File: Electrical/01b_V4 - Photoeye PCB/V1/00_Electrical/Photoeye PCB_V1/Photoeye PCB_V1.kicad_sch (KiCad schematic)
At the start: 13 parts, among them J1 B3B-PH-SM4-TB(LF)(SN), J2 B3B-PH-SM4-TB(LF)(SN), U1 LM293ST, U2 RPR-220

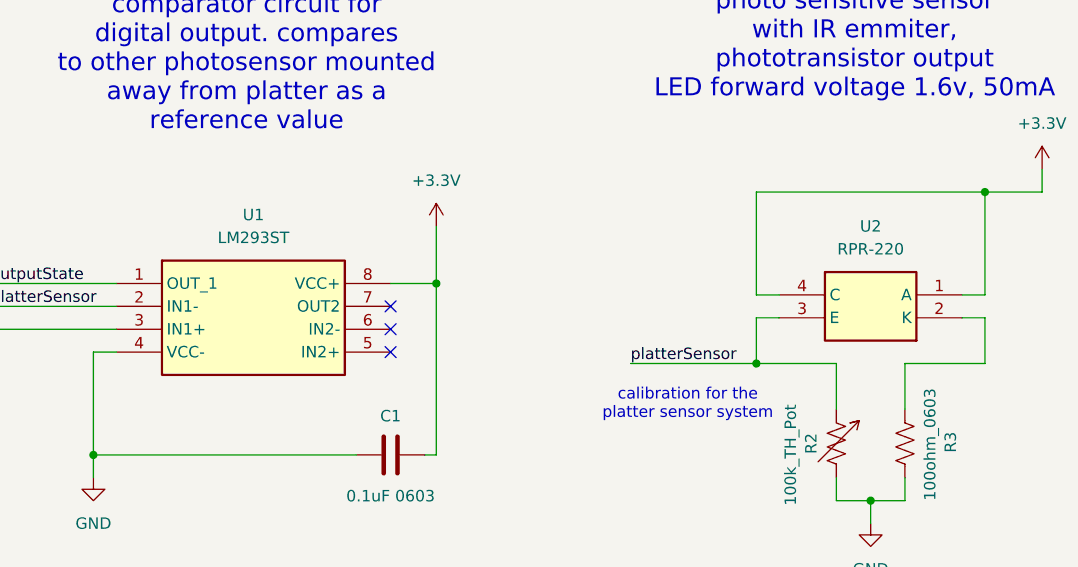
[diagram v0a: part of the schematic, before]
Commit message: fixing the crossed wire for the photo sensor. deleting the old CNC jobs. Re-exporting gerbers and schematics. Re-mill with new files
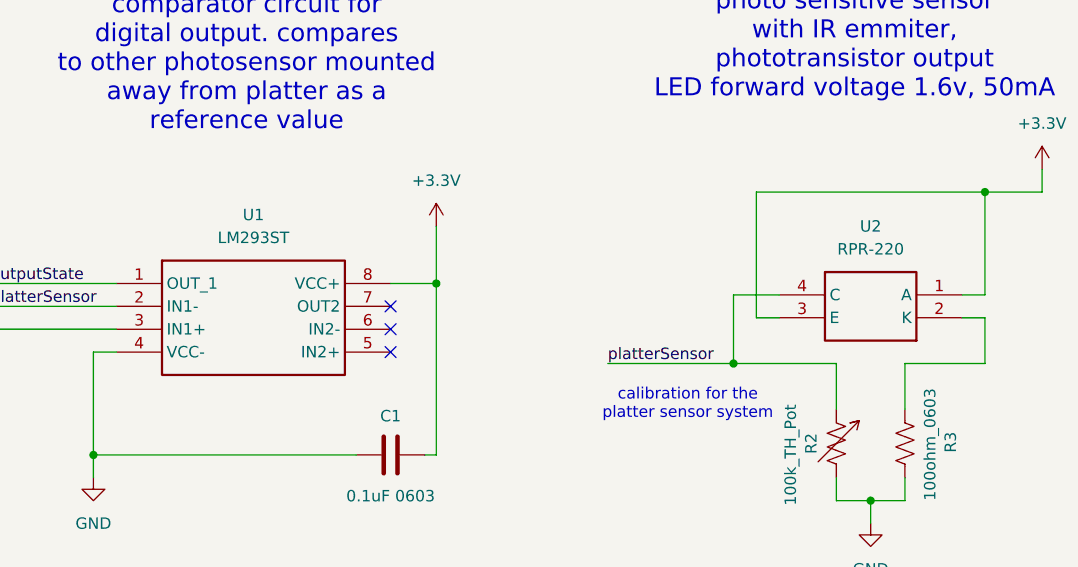
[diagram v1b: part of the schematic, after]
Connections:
- net +3.3V: now also U2.3 (E); no longer U2.4 (C)
- net platterSensor: now also U2.4 (C); no longer U2.3 (E)
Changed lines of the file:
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@@
 	)
 	(junction
-		(at 198.12 68.58)
+		(at 170.18 87.63)
 		(diameter 0)
 		(color 0 0 0 0)
 	)
 	(junction
-		(at 172.72 87.63)
+		(at 198.12 68.58)
 		(diameter 0)
 		(color 0 0 0 0)
@@
 	(wire
 		(pts
+			(xy 172.72 82.55) (xy 175.26 82.55)
+		)
+		(stroke
+			(width 0)
+			(type default)
+		)
+	)
+	(wire
+		(pts
 			(xy 227.33 81.28) (xy 227.33 86.36)
 		)
@@
 	(wire
 		(pts
-			(xy 101.6 86.36) (xy 99.06 86.36)
+			(xy 172.72 68.58) (xy 172.72 82.55)
 		)
 		(stroke
@@
 	(wire
 		(pts
-			(xy 238.76 60.96) (xy 238.76 73.66)
+			(xy 101.6 86.36) (xy 99.06 86.36)
 		)
 		(stroke
@@
 	(wire
 		(pts
-			(xy 49.53 76.2) (xy 49.53 71.12)
+			(xy 238.76 60.96) (xy 238.76 73.66)
 		)
 		(stroke
@@
 	(wire
 		(pts
-			(xy 172.72 87.63) (xy 181.61 87.63)
+			(xy 49.53 76.2) (xy 49.53 71.12)
 		)
 		(stroke
@@
 	(wire
 		(pts
-			(xy 172.72 80.01) (xy 172.72 68.58)
+			(xy 175.26 80.01) (xy 170.18 80.01)
 		)
 		(stroke
@@
 	(wire
 		(pts
-			(xy 175.26 82.55) (xy 172.72 82.55)
+			(xy 219.71 95.25) (xy 219.71 101.6)
 		)
 		(stroke
@@
 	(wire
 		(pts
-			(xy 219.71 95.25) (xy 219.71 101.6)
+			(xy 198.12 87.63) (xy 189.23 87.63)
 		)
 		(stroke
@@
 	(wire
 		(pts
-			(xy 198.12 87.63) (xy 189.23 87.63)
+			(xy 156.21 87.63) (xy 170.18 87.63)
 		)
 		(stroke
@@
 	(wire
 		(pts
-			(xy 158.75 87.63) (xy 172.72 87.63)
+			(xy 170.18 80.01) (xy 170.18 87.63)
 		)
 		(stroke
@@
 	(wire
 		(pts
-			(xy 172.72 82.55) (xy 172.72 87.63)
+			(xy 172.72 68.58) (xy 198.12 68.58)
 		)
 		(stroke
@@
 	(wire
 		(pts
-			(xy 172.72 68.58) (xy 198.12 68.58)
+			(xy 46.99 73.66) (xy 52.07 73.66)
 		)
 		(stroke
@@
 	(wire
 		(pts
-			(xy 46.99 73.66) (xy 52.07 73.66)
+			(xy 170.18 87.63) (xy 181.61 87.63)
 		)
 		(stroke
@@
 	(wire
 		(pts
-			(xy 175.26 80.01) (xy 172.72 80.01)
-		)
-		(stroke
-			(width 0)
-			(type default)
-		)
-	)
-	(wire
-		(pts
 			(xy 52.07 73.66) (xy 52.07 78.74)
 		)
@@
 	)
 	(label "platterSensor"
-		(at 158.75 87.63 0)
+		(at 156.21 87.63 0)
 		(effects
 			(font

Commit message: updates and cnc files to photo eye pcbs
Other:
- note added: "This is the Platter Detection System for the Zoetrope Carousel V4. The system uses two photo-sensitive sensors (RPR-220) and a comparator to determine if a platter is loaded on the machine or not. One sensor lives on this PCB, the other on a separate PCB that connects to this PCB via connector J2. The two sensors must be mounted away from eachother. This sensor and PCB must be mounted beneith the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"
- note added: "calibration for the platter sensor system ADD BEHAVIOR HERE AFTER TESTING higher value should decrease? sensitivity"
- note added: "calibration for the platter sensor system higher value increases sensing distance"
- note added: "comparator circuit for digital output. compares the two photosensors to determine if platter is present on machine"
- note added: "connector to reference sensor (ambient light reference mounted away from platter)"
- note added: "no platter"
- note added: "photo sensitive sensor with IR emmiter, phototransistor p-chanel output LED forward voltage 1.6v, 50mA 0.5uA (dark) to 0.8mA (light) (platter sensor, mounted beneath machine platter)"
- note added: "platter present"
- note removed: "calibration for the platter sensor system"
- note removed: "comparator circuit for digital output. compares to other photosensor mounted away from platter as a reference value"
- note removed: "connector to reference sensor (ambient light reference)"
- note removed: "photo sensitive sensor with IR emmiter, phototransistor output LED forward voltage 1.6v, 50mA"

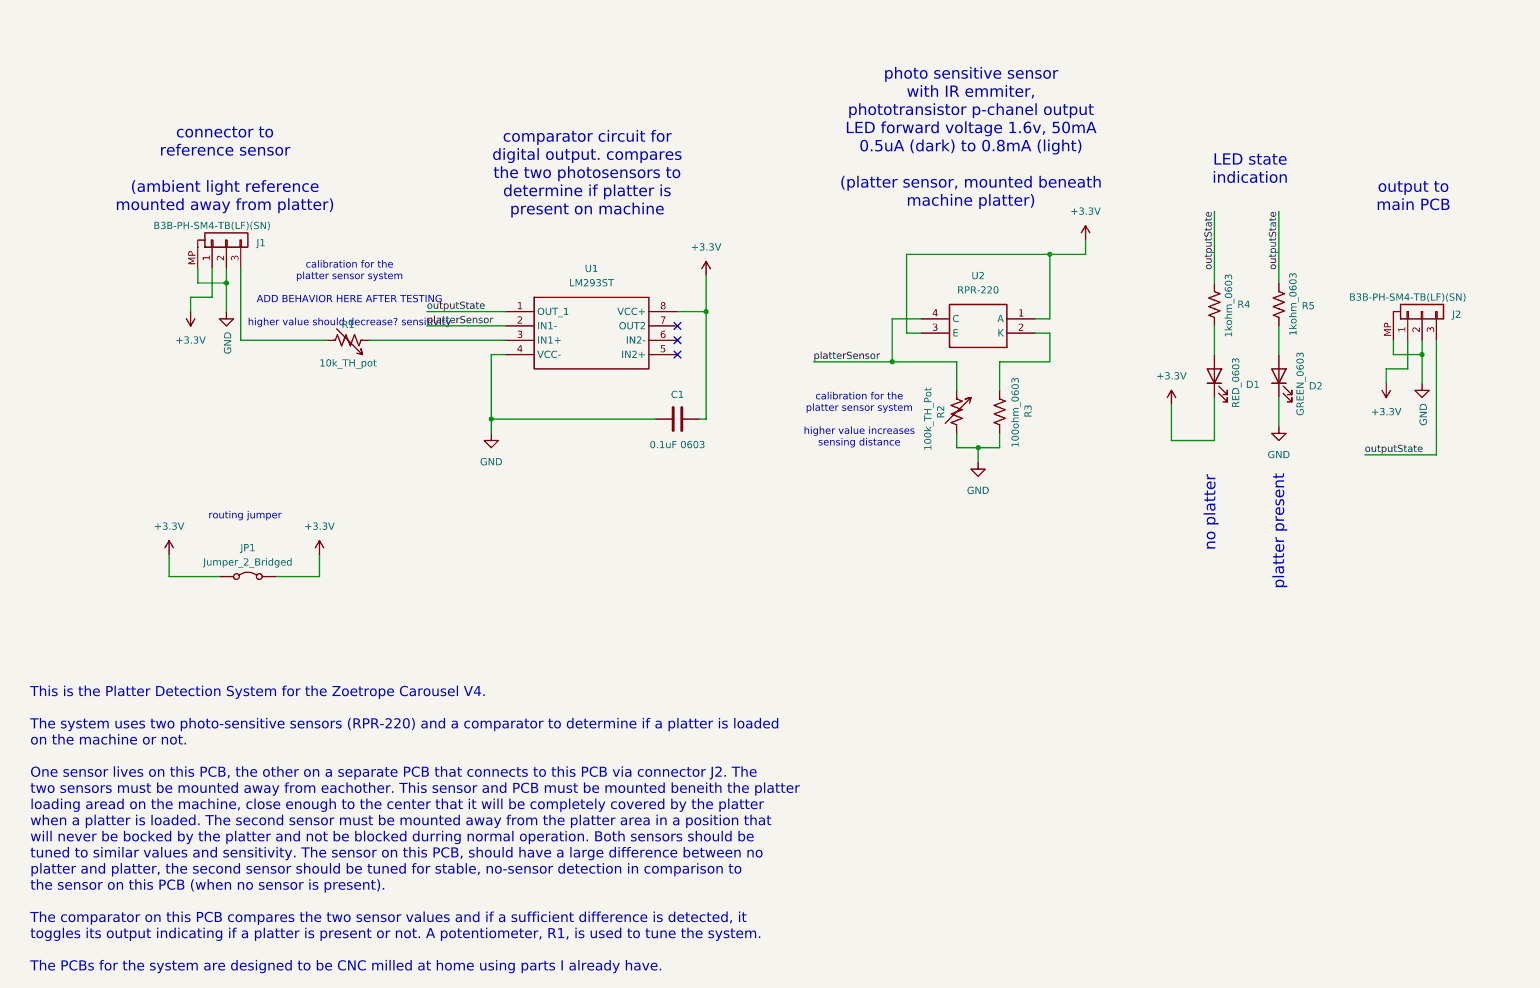
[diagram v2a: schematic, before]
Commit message: updates to schematic to document outside components. Plans for additional electrical features requiring desiging a few more PCBs
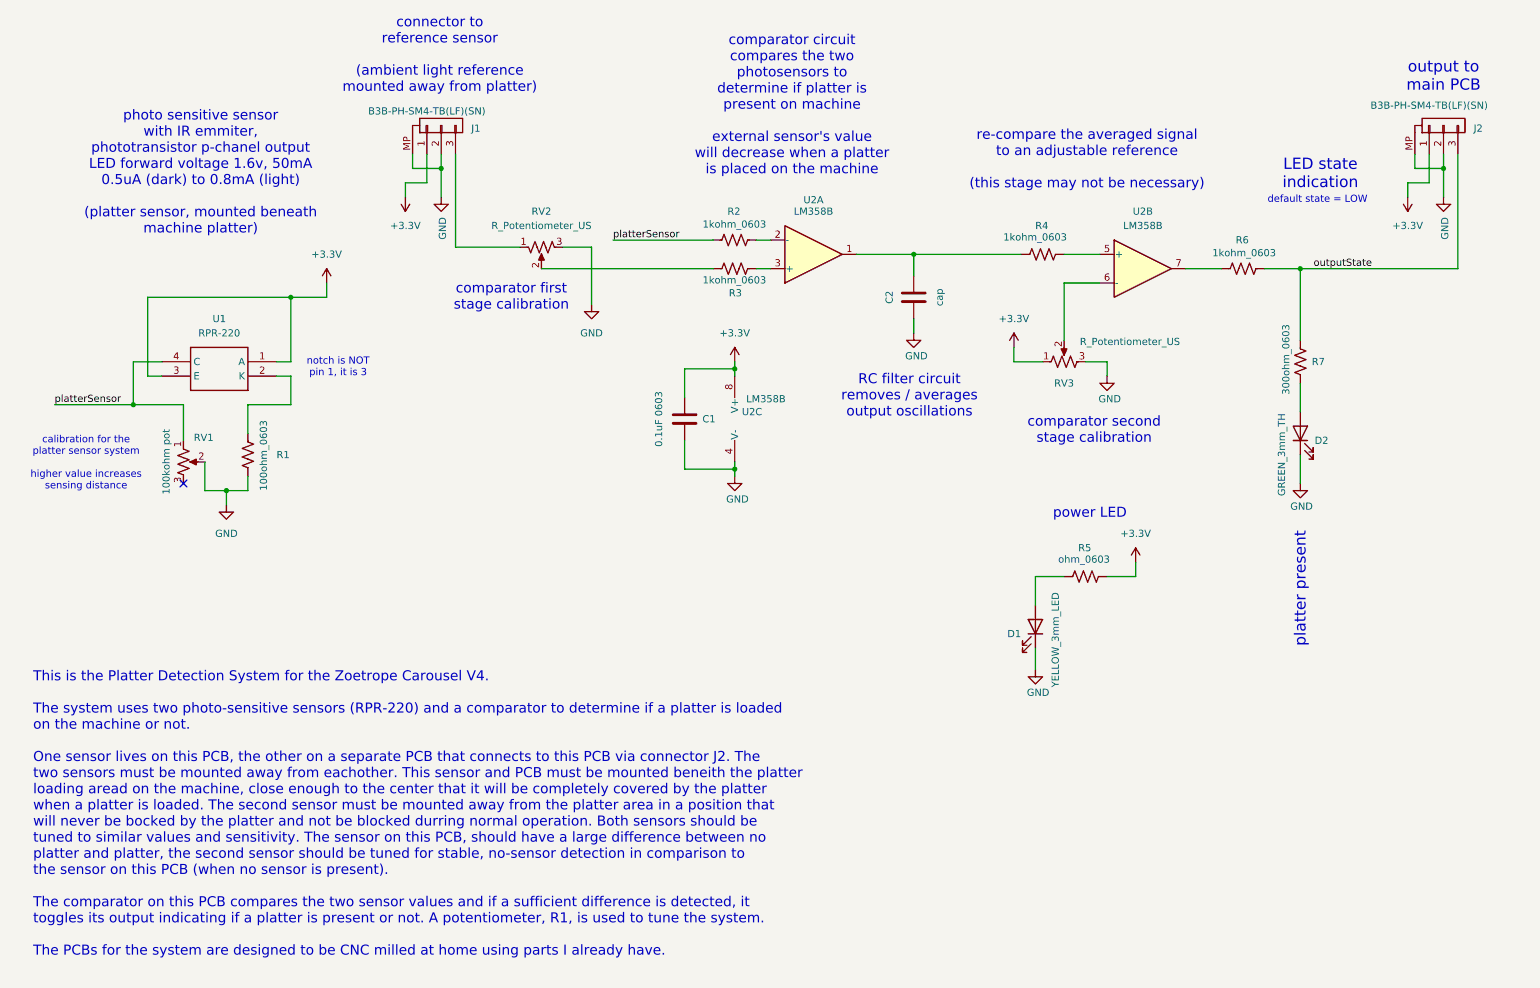
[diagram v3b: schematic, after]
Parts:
- removed D2: GREEN_0603, LED_SMD:LED_0603_1608Metric, symbol Device:LED
- removed JP1: Jumper_2_Bridged, photoeye_pcb:3mm jumper, symbol Jumper:Jumper_2_Bridged
- removed R1: 10k_TH_pot, photoeye_pcb:Potentiometer_TH, symbol Device:R_Variable_US
- removed R2: 100k_TH_Pot, photoeye_pcb:Potentiometer_TH, symbol Device:R_Variable_US
- removed U1: LM293ST, photoeye_pcb:LM293ST, symbol photoeye_PCB:LM293ST
- added C2: cap, Capacitor_SMD:C_0603_1608Metric, symbol Device:C
- added D1: YELLOW_3mm_LED, LED_THT:LED_D3.0mm_Clear, symbol Device:LED
- added R2, R3, R6: 1kohm_0603, Resistor_SMD:R_0603_1608Metric, symbol Device:R_US
- added R5: ohm_0603, Resistor_SMD:R_0603_1608Metric, symbol Device:R_US
- added RV1: 100kohm pot, Potentiometer_THT:Potentiometer_Bourns_3296W_Vertical, symbol Device:R_Potentiometer_US
- added RV2, RV3: R_Potentiometer_US, Potentiometer_THT:Potentiometer_Bourns_3296W_Vertical, symbol Device:R_Potentiometer_US
- added U2: LM358B, Package_TO_SOT_SMD:SOT-23-8, symbol Amplifier_Operational:LM358
- D2: renamed from D1; value RED_0603 -> GREEN_3mm_TH; footprint LED_SMD:LED_0603_1608Metric -> LED_THT:LED_D3.0mm
- R7: renamed from R5; value 1kohm_0603 -> 300ohm_0603
- renumbered R3 to R1, U2 to U1
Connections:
- net +3.3V: now also C1.1, R5.1, RV3.1, U2.8 (V+); no longer C1.2, D2.1 (K)
- net GND: now also C1.2, D2.1 (K), C2.1, D1.1 (K), RV1.2, RV2.3, RV3.3, U2.4 (V-); no longer C1.1
- net outputState: now also R6.1; no longer R4.2
- net platterSensor: now also R2.2, RV1.1
- net at R7.1: now also D2.2 (A)
- net at J1.3 (Pin_3): now also RV2.1
- net at R4.1: now also U2.5 (+); no longer D2.2 (A)
- new net: RV3.2, U2.6 (-)
- new net: R6.2, U2.7
- new net: C2.2, R4.2, U2.1
- new net: R3.1, U2.3 (+)
- new net: R3.2, RV2.2
- new net: D1.2 (A), R5.2
- new net: R2.1, U2.2 (-)
- no-connect marks 3 -> 1
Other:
- note added: "RC filter circuit removes / averages output oscillations"
- note added: "comparator circuit compares the two photosensors to determine if platter is present on machine external sensor's value will decrease when a platter is placed on the machine"
- note added: "comparator first stage calibration"
- note added: "comparator second stage calibration"
- note added: "default state = LOW"
- note added: "notch is NOT pin 1, it is 3"
- note added: "power LED"
- note added: "re-compare the averaged signal to an adjustable reference (this stage may not be necessary)"
- note removed: "calibration for the platter sensor system ADD BEHAVIOR HERE AFTER TESTING higher value should decrease? sensitivity"
- note removed: "comparator circuit for digital output. compares the two photosensors to determine if platter is present on machine"
- note removed: "no platter"
- note removed: "routing jumper"
- moved on the sheet: C1, D2, J1, J2, R1, R7, U1
